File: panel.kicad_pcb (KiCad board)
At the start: 2 copper layers, 96 x 88.1 mm, 272 parts, among them J1 Terminal, J10 Terminal, J11 Conn_01x02_Socket, J12 Conn_01x02_Socket, J13 Terminal, J14 Conn_01x02_Socket, J15 Conn_01x02_Socket, J16 Terminal, J17 Conn_01x02_Socket, J18 Conn_01x02_Socket, J19 Terminal, J2 Conn_01x02_Socket, J20 Conn_01x02_Socket, J21 Conn_01x02_Socket, J22 Terminal, J23 Conn_01x02_Socket, J24 Conn_01x02_Socket, J25 Terminal, J26 Conn_01x02_Socket, J27 Conn_01x02_Socket, J28 Terminal, J29 Conn_01x02_Socket, J3 Conn_01x02_Socket, J30 Conn_01x02_Socket, J31 Terminal, J32 Conn_01x02_Socket, J33 Conn_01x02_Socket, J34 Terminal, J35 Conn_01x02_Socket, J36 Conn_01x02_Socket, J37 Terminal, J38 Conn_01x02_Socket, J39 Conn_01x02_Socket, J4 Terminal, J40 Terminal, J41 Conn_01x02_Socket, J42 Conn_01x02_Socket, J43 Terminal, J44 Conn_01x02_Socket, J45 Conn_01x02_Socket, J46 Terminal, J47 Conn_01x02_Socket, J48 Conn_01x02_Socket, J5 Conn_01x02_Socket, J6 Conn_01x02_Socket, J7 Terminal, J8 Conn_01x02_Socket, J9 Conn_01x02_Socket, M10 MountingHole_3.2mm_M3_Pad_Via, M11 MountingHole_3.2mm_M3_Pad_Via, M12 MountingHole_3.2mm_M3_Pad_Via, M13 MountingHole_3.2mm_M3_Pad_Via, M14 MountingHole_3.2mm_M3_Pad_Via, M15 MountingHole_3.2mm_M3_Pad_Via, M16 MountingHole_3.2mm_M3_Pad_Via, M17 MountingHole_3.2mm_M3_Pad_Via, M18 MountingHole_3.2mm_M3_Pad_Via, M19 MountingHole_3.2mm_M3_Pad_Via, M20 MountingHole_3.2mm_M3_Pad_Via, M21 MountingHole_3.2mm_M3_Pad_Via, M22 MountingHole_3.2mm_M3_Pad_Via, M23 MountingHole_3.2mm_M3_Pad_Via, M24 MountingHole_3.2mm_M3_Pad_Via, M25 MountingHole_3.2mm_M3_Pad_Via, M26 MountingHole_3.2mm_M3_Pad_Via, M27 MountingHole_3.2mm_M3_Pad_Via, M28 MountingHole_3.2mm_M3_Pad_Via, M29 MountingHole_3.2mm_M3_Pad_Via, M3 MountingHole_3.2mm_M3_Pad_Via, M30 MountingHole_3.2mm_M3_Pad_Via, M31 MountingHole_3.2mm_M3_Pad_Via, M32 MountingHole_3.2mm_M3_Pad_Via, M33 MountingHole_3.2mm_M3_Pad_Via, M4 MountingHole_3.2mm_M3_Pad_Via, M5 MountingHole_3.2mm_M3_Pad_Via, M6 MountingHole_3.2mm_M3_Pad_Via, M7 MountingHole_3.2mm_M3_Pad_Via, M8 MountingHole_3.2mm_M3_Pad_Via, M9 MountingHole_3.2mm_M3_Pad_Via, Q1 CSD17578Q5A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

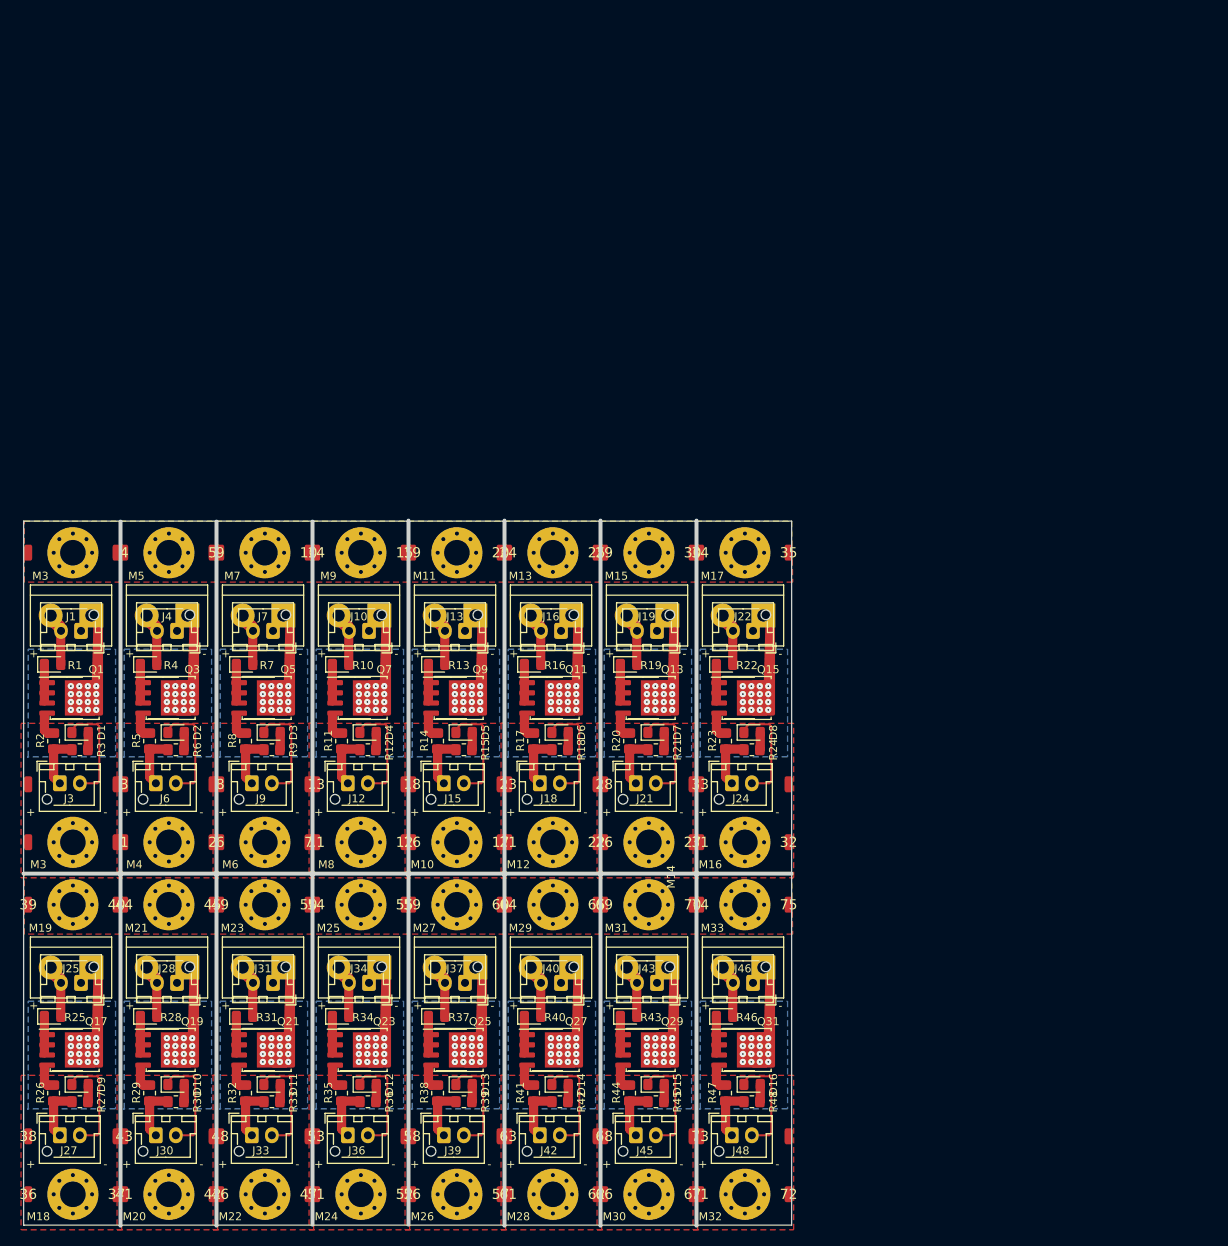
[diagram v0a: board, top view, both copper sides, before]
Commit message: update panelized PCB
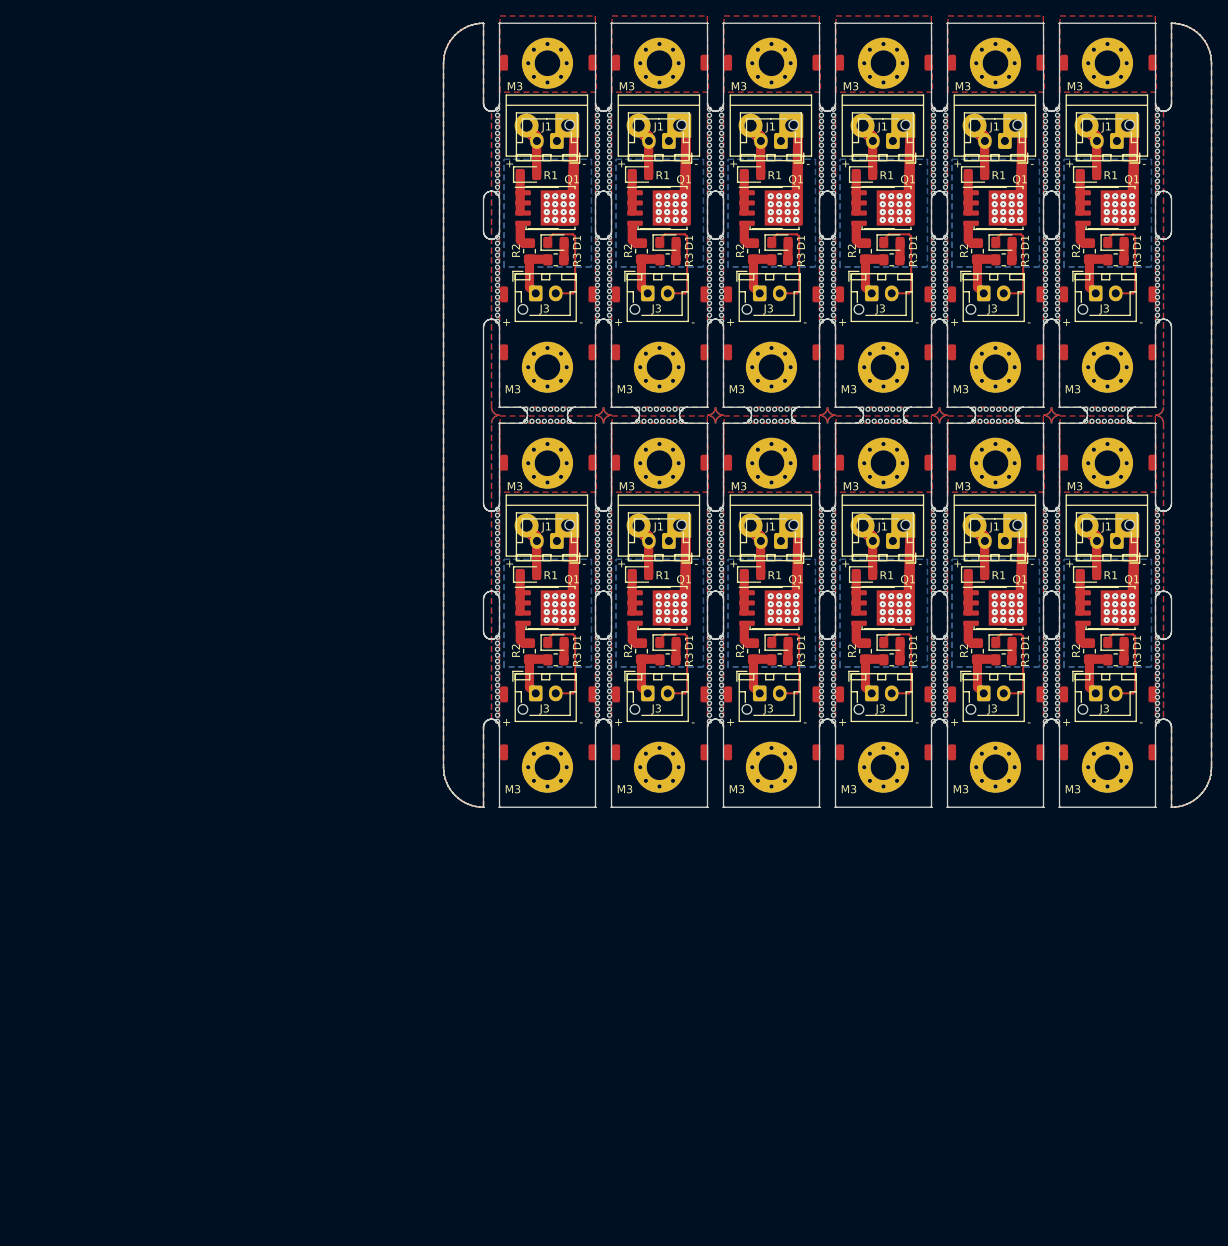
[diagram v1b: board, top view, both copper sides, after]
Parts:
- removed 1, 10, 11, 12, 13, 14, 15, 16, 17, 18, 19, 2, 20, 21, 22, 23, 24, 25, 26, 27, 28, 29, 3, 30, 31, 32, 33, 34, 35, 36, 37, 38, 39, 4, 40, 41, 42, 43, 44, 45, 46, 47, 48, 49, 5, 50, 51, 52, 53, 54, 55, 56, 57, 58, 59, 6, 60, 61, 62, 63, 64, 65, 66, 67, 68, 69, 7, 70, 71, 72, 73, 74, 75, 8, 9: , 
- removed the ? at (48.6, 122.4)
- removed the ? at (48.6, 115.1)
- removed the ? at (59.6, 122.4)
- removed the ? at (48.6, 86.2)
- removed the ? at (59.6, 86.2)
- removed the D1 at (55.1, 108.7)
- removed D10, D11, D12, D13, D14, D15, D16, D2, D3, D4, D5, D6, D7, D8, D9: LED, LED_SMD:LED_0805_2012Metric_Pad1.15x1.40mm_HandSolder
- removed the J1 at (56.5, 94.0)
- removed J10, J13, J16, J19, J22, J25, J28, J31, J34, J37, J4, J40, J43, J46, J7: Terminal, TerminalBlock:TerminalBlock_bornier-2_P5.08mm
- removed J11, J12, J14, J15, J17, J18, J20, J21, J23, J24, J26, J27, J29, J30, J32, J33, J35, J36, J38, J39, J41, J42, J44, J45, J47, J48, J5, J6, J8, J9: Conn_01x02_Socket, Connector_JST:JST_XH_B2B-XH-AM_1x02_P2.50mm_Vertical
- removed the J2 at (55.2, 96.0)
- removed the J3 at (52.5, 115.0)
- removed M10, M11, M12, M13, M14, M15, M16, M17, M18, M19, M20, M21, M22, M23, M24, M25, M26, M27, M28, M29, M30, M31, M32, M33, M4, M5, M6, M7, M8, M9: MountingHole_3.2mm_M3_Pad_Via, MountingHole:MountingHole_3.2mm_M3_Pad_Via
- removed the M3 at (54.2, 122.4)
- removed the M3 at (54.2, 86.2)
- removed the Q1 at (54.4, 104.3)
- removed Q10, Q12, Q14, Q16, Q18, Q20, Q22, Q24, Q26, Q28, Q30, Q32, Q4, Q6, Q8: CSD17578Q5A, Package_SO:SOP-8_3.76x4.96mm_P1.27mm
- removed Q11, Q13, Q15, Q17, Q19, Q21, Q23, Q25, Q27, Q29, Q3, Q31, Q5, Q7, Q9: CSD17578Q5A, Package_TO_SOT_SMD:TDSON-8-1
- removed the Q2 at (53.5, 104.3)
- removed the R1 at (51.6, 100.1)
- removed R10, R13, R16, R19, R22, R25, R28, R31, R34, R37, R4, R40, R43, R46, R7: R, LED_SMD:LED_0805_2012Metric_Pad1.15x1.40mm_HandSolder
- removed R11, R12, R14, R15, R17, R18, R20, R21, R23, R24, R26, R27, R29, R30, R32, R33, R35, R36, R38, R39, R41, R42, R44, R45, R47, R48, R5, R6, R8, R9: R, Resistor_SMD:R_0805_2012Metric_Pad1.20x1.40mm_HandSolder
- removed the R2 at (51.8, 109.7)
- removed the R3 at (55.0, 110.8)
- removed the REF** at (59.6, 115.1)
- removed REF**1, REF**10, REF**11, REF**12, REF**13, REF**14, REF**15, REF**2, REF**3, REF**4, REF**5, REF**6, REF**7, REF**8, REF**9: SolderWirePad_1x01_SMD_1x2mm, Connector_Wire:SolderWirePad_1x01_SMD_1x2mm
- added ?: , , F.Cu at (108.1, 53.9)
- added ?: , , F.Cu at (164.1, 74.9)
- added ?: , , F.Cu at (136.1, 103.9)
- added ?: , , F.Cu at (133.1, 74.9)
- added ?: , , F.Cu at (161.1, 111.1)
- added ?: , , F.Cu at (164.1, 24.9)
- added ?: , , F.Cu at (108.1, 74.9)
- added ?: , , F.Cu at (147.1, 61.1)
- added ?: , , F.Cu at (122.1, 24.9)
- added ?: , , F.Cu at (161.1, 61.1)
- added ?: , , F.Cu at (189.1, 111.1)
- added ?: , , F.Cu at (178.1, 111.1)
- added ?: , , F.Cu at (178.1, 74.9)
- added ?: , , F.Cu at (119.1, 61.1)
- added ?: , , F.Cu at (150.1, 74.9)
- added ?: , , F.Cu at (164.1, 53.9)
- added ?: , , F.Cu at (178.1, 103.9)
- added ?: , , F.Cu at (136.1, 74.9)
- added ?: , , F.Cu at (164.1, 103.9)
- added ?: , , F.Cu at (175.1, 61.1)
- added ?: , , F.Cu at (122.1, 61.1)
- added ?: , , F.Cu at (119.1, 24.9)
- added ?: , , F.Cu at (122.1, 111.1)
- added ?: , , F.Cu at (175.1, 74.9)
- added ?: , , F.Cu at (189.1, 61.1)
- added ?: , , F.Cu at (189.1, 24.9)
- added ?: , , F.Cu at (178.1, 61.1)
- added ?: , , F.Cu at (122.1, 103.9)
- added ?: , , F.Cu at (164.1, 61.1)
- added ?: , , F.Cu at (119.1, 111.1)
- added ?: , , F.Cu at (108.1, 111.1)
- added ?: , , F.Cu at (189.1, 74.9)
- added ?: , , F.Cu at (133.1, 24.9)
- added ?: , , F.Cu at (147.1, 24.9)
- added ?: , , F.Cu at (136.1, 61.1)
- added ?: , , F.Cu at (133.1, 111.1)
- added ?: , , F.Cu at (147.1, 111.1)
- added ?: , , F.Cu at (150.1, 61.1)
- added ?: , , F.Cu at (122.1, 74.9)
- added ?: , , F.Cu at (175.1, 24.9)
- added ?: , , F.Cu at (119.1, 74.9)
- added ?: , , F.Cu at (108.1, 103.9)
- added ?: , , F.Cu at (150.1, 111.1)
- added ?: , , F.Cu at (178.1, 53.9)
- added ?: , , F.Cu at (164.1, 111.1)
- added ?: , , F.Cu at (136.1, 53.9)
- added ?: , , F.Cu at (136.1, 111.1)
- added ?: , , F.Cu at (108.1, 24.9)
- added ?: , , F.Cu at (122.1, 53.9)
- added ?: , , F.Cu at (147.1, 74.9)
- added ?: , , F.Cu at (161.1, 74.9)
- added ?: , , F.Cu at (133.1, 61.1)
- added ?: , , F.Cu at (161.1, 24.9)
- added ?: , , F.Cu at (150.1, 103.9)
- added ?: , , F.Cu at (136.1, 24.9)
- added ?: , , F.Cu at (178.1, 24.9)
- added ?: , , F.Cu at (108.1, 61.1)
- added ?: , , F.Cu at (175.1, 111.1)
- added ?: , , F.Cu at (150.1, 24.9)
- added ?: , , F.Cu at (150.1, 53.9)
- added D1: LED, LED_SMD:LED_0805_2012Metric_Pad1.15x1.40mm_HandSolder, F.Cu at (114.6, 47.4)
- added D1: LED, LED_SMD:LED_0805_2012Metric_Pad1.15x1.40mm_HandSolder, F.Cu at (156.6, 97.4)
- added D1: LED, LED_SMD:LED_0805_2012Metric_Pad1.15x1.40mm_HandSolder, F.Cu at (184.6, 97.4)
- added D1: LED, LED_SMD:LED_0805_2012Metric_Pad1.15x1.40mm_HandSolder, F.Cu at (114.6, 97.4)
- added D1: LED, LED_SMD:LED_0805_2012Metric_Pad1.15x1.40mm_HandSolder, F.Cu at (170.6, 47.4)
- added D1: LED, LED_SMD:LED_0805_2012Metric_Pad1.15x1.40mm_HandSolder, F.Cu at (156.6, 47.4)
- added D1: LED, LED_SMD:LED_0805_2012Metric_Pad1.15x1.40mm_HandSolder, F.Cu at (184.6, 47.4)
- added D1: LED, LED_SMD:LED_0805_2012Metric_Pad1.15x1.40mm_HandSolder, F.Cu at (128.6, 97.4)
- added D1: LED, LED_SMD:LED_0805_2012Metric_Pad1.15x1.40mm_HandSolder, F.Cu at (142.6, 47.4)
- added D1: LED, LED_SMD:LED_0805_2012Metric_Pad1.15x1.40mm_HandSolder, F.Cu at (142.6, 97.4)
- added D1: LED, LED_SMD:LED_0805_2012Metric_Pad1.15x1.40mm_HandSolder, F.Cu at (128.6, 47.4)
- added D1: LED, LED_SMD:LED_0805_2012Metric_Pad1.15x1.40mm_HandSolder, F.Cu at (170.6, 97.4)
- added J1: Terminal, TerminalBlock:TerminalBlock_bornier-2_P5.08mm, F.Cu at (144.0, 32.8)
- added J1: Terminal, TerminalBlock:TerminalBlock_bornier-2_P5.08mm, F.Cu at (158.0, 32.8)
- added J1: Terminal, TerminalBlock:TerminalBlock_bornier-2_P5.08mm, F.Cu at (116.0, 32.8)
- added J1: Terminal, TerminalBlock:TerminalBlock_bornier-2_P5.08mm, F.Cu at (172.0, 82.8)
- added J1: Terminal, TerminalBlock:TerminalBlock_bornier-2_P5.08mm, F.Cu at (186.0, 82.8)
- added J1: Terminal, TerminalBlock:TerminalBlock_bornier-2_P5.08mm, F.Cu at (158.0, 82.8)
- added J1: Terminal, TerminalBlock:TerminalBlock_bornier-2_P5.08mm, F.Cu at (172.0, 32.8)
- added J1: Terminal, TerminalBlock:TerminalBlock_bornier-2_P5.08mm, F.Cu at (130.0, 32.8)
- added J1: Terminal, TerminalBlock:TerminalBlock_bornier-2_P5.08mm, F.Cu at (186.0, 32.8)
- added J1: Terminal, TerminalBlock:TerminalBlock_bornier-2_P5.08mm, F.Cu at (116.0, 82.8)
- added J1: Terminal, TerminalBlock:TerminalBlock_bornier-2_P5.08mm, F.Cu at (130.0, 82.8)
- added J1: Terminal, TerminalBlock:TerminalBlock_bornier-2_P5.08mm, F.Cu at (144.0, 82.8)
- added J2: Conn_01x02_Socket, Connector_JST:JST_XH_B2B-XH-AM_1x02_P2.50mm_Vertical, F.Cu at (184.7, 84.7)
- added J2: Conn_01x02_Socket, Connector_JST:JST_XH_B2B-XH-AM_1x02_P2.50mm_Vertical, F.Cu at (170.7, 34.7)
- added J2: Conn_01x02_Socket, Connector_JST:JST_XH_B2B-XH-AM_1x02_P2.50mm_Vertical, F.Cu at (128.7, 34.7)
- added J2: Conn_01x02_Socket, Connector_JST:JST_XH_B2B-XH-AM_1x02_P2.50mm_Vertical, F.Cu at (156.7, 34.7)
- added J2: Conn_01x02_Socket, Connector_JST:JST_XH_B2B-XH-AM_1x02_P2.50mm_Vertical, F.Cu at (156.7, 84.7)
- added J2: Conn_01x02_Socket, Connector_JST:JST_XH_B2B-XH-AM_1x02_P2.50mm_Vertical, F.Cu at (142.7, 84.7)
- added J2: Conn_01x02_Socket, Connector_JST:JST_XH_B2B-XH-AM_1x02_P2.50mm_Vertical, F.Cu at (114.7, 34.7)
- added J2: Conn_01x02_Socket, Connector_JST:JST_XH_B2B-XH-AM_1x02_P2.50mm_Vertical, F.Cu at (142.7, 34.7)
- added J2: Conn_01x02_Socket, Connector_JST:JST_XH_B2B-XH-AM_1x02_P2.50mm_Vertical, F.Cu at (128.7, 84.7)
- added J2: Conn_01x02_Socket, Connector_JST:JST_XH_B2B-XH-AM_1x02_P2.50mm_Vertical, F.Cu at (170.7, 84.7)
- added J2: Conn_01x02_Socket, Connector_JST:JST_XH_B2B-XH-AM_1x02_P2.50mm_Vertical, F.Cu at (114.7, 84.7)
- added J2: Conn_01x02_Socket, Connector_JST:JST_XH_B2B-XH-AM_1x02_P2.50mm_Vertical, F.Cu at (184.7, 34.7)
- added J3: Conn_01x02_Socket, Connector_JST:JST_XH_B2B-XH-AM_1x02_P2.50mm_Vertical, F.Cu at (154.0, 103.8)
- added J3: Conn_01x02_Socket, Connector_JST:JST_XH_B2B-XH-AM_1x02_P2.50mm_Vertical, F.Cu at (112.0, 103.8)
- added J3: Conn_01x02_Socket, Connector_JST:JST_XH_B2B-XH-AM_1x02_P2.50mm_Vertical, F.Cu at (112.0, 53.8)
- added J3: Conn_01x02_Socket, Connector_JST:JST_XH_B2B-XH-AM_1x02_P2.50mm_Vertical, F.Cu at (126.0, 103.8)
- added J3: Conn_01x02_Socket, Connector_JST:JST_XH_B2B-XH-AM_1x02_P2.50mm_Vertical, F.Cu at (154.0, 53.8)
- added J3: Conn_01x02_Socket, Connector_JST:JST_XH_B2B-XH-AM_1x02_P2.50mm_Vertical, F.Cu at (140.0, 53.8)
- added J3: Conn_01x02_Socket, Connector_JST:JST_XH_B2B-XH-AM_1x02_P2.50mm_Vertical, F.Cu at (168.0, 103.8)
- added J3: Conn_01x02_Socket, Connector_JST:JST_XH_B2B-XH-AM_1x02_P2.50mm_Vertical, F.Cu at (168.0, 53.8)
- added J3: Conn_01x02_Socket, Connector_JST:JST_XH_B2B-XH-AM_1x02_P2.50mm_Vertical, F.Cu at (182.0, 53.8)
- added J3: Conn_01x02_Socket, Connector_JST:JST_XH_B2B-XH-AM_1x02_P2.50mm_Vertical, F.Cu at (126.0, 53.8)
- added J3: Conn_01x02_Socket, Connector_JST:JST_XH_B2B-XH-AM_1x02_P2.50mm_Vertical, F.Cu at (140.0, 103.8)
- added J3: Conn_01x02_Socket, Connector_JST:JST_XH_B2B-XH-AM_1x02_P2.50mm_Vertical, F.Cu at (182.0, 103.8)
- added M3: MountingHole_3.2mm_M3_Pad_Via, MountingHole:MountingHole_3.2mm_M3_Pad_Via, F.Cu at (113.5, 63.0)
- added M3: MountingHole_3.2mm_M3_Pad_Via, MountingHole:MountingHole_3.2mm_M3_Pad_Via, F.Cu at (183.5, 113.0)
- added M3: MountingHole_3.2mm_M3_Pad_Via, MountingHole:MountingHole_3.2mm_M3_Pad_Via, F.Cu at (113.5, 113.0)
- added M3: MountingHole_3.2mm_M3_Pad_Via, MountingHole:MountingHole_3.2mm_M3_Pad_Via, F.Cu at (155.5, 113.0)
- added M3: MountingHole_3.2mm_M3_Pad_Via, MountingHole:MountingHole_3.2mm_M3_Pad_Via, F.Cu at (155.5, 75.0)
- added M3: MountingHole_3.2mm_M3_Pad_Via, MountingHole:MountingHole_3.2mm_M3_Pad_Via, F.Cu at (169.5, 63.0)
- added M3: MountingHole_3.2mm_M3_Pad_Via, MountingHole:MountingHole_3.2mm_M3_Pad_Via, F.Cu at (113.5, 75.0)
- added M3: MountingHole_3.2mm_M3_Pad_Via, MountingHole:MountingHole_3.2mm_M3_Pad_Via, F.Cu at (183.5, 25.0)
- added M3: MountingHole_3.2mm_M3_Pad_Via, MountingHole:MountingHole_3.2mm_M3_Pad_Via, F.Cu at (127.5, 113.0)
- added M3: MountingHole_3.2mm_M3_Pad_Via, MountingHole:MountingHole_3.2mm_M3_Pad_Via, F.Cu at (155.5, 25.0)
- added M3: MountingHole_3.2mm_M3_Pad_Via, MountingHole:MountingHole_3.2mm_M3_Pad_Via, F.Cu at (127.5, 75.0)
- added M3: MountingHole_3.2mm_M3_Pad_Via, MountingHole:MountingHole_3.2mm_M3_Pad_Via, F.Cu at (127.5, 63.0)
- added M3: MountingHole_3.2mm_M3_Pad_Via, MountingHole:MountingHole_3.2mm_M3_Pad_Via, F.Cu at (169.5, 75.0)
- added M3: MountingHole_3.2mm_M3_Pad_Via, MountingHole:MountingHole_3.2mm_M3_Pad_Via, F.Cu at (183.5, 63.0)
- added M3: MountingHole_3.2mm_M3_Pad_Via, MountingHole:MountingHole_3.2mm_M3_Pad_Via, F.Cu at (183.5, 75.0)
- added M3: MountingHole_3.2mm_M3_Pad_Via, MountingHole:MountingHole_3.2mm_M3_Pad_Via, F.Cu at (127.5, 25.0)
- added M3: MountingHole_3.2mm_M3_Pad_Via, MountingHole:MountingHole_3.2mm_M3_Pad_Via, F.Cu at (141.5, 25.0)
- added M3: MountingHole_3.2mm_M3_Pad_Via, MountingHole:MountingHole_3.2mm_M3_Pad_Via, F.Cu at (169.5, 113.0)
- added M3: MountingHole_3.2mm_M3_Pad_Via, MountingHole:MountingHole_3.2mm_M3_Pad_Via, F.Cu at (169.5, 25.0)
- added M3: MountingHole_3.2mm_M3_Pad_Via, MountingHole:MountingHole_3.2mm_M3_Pad_Via, F.Cu at (141.5, 113.0)
- added M3: MountingHole_3.2mm_M3_Pad_Via, MountingHole:MountingHole_3.2mm_M3_Pad_Via, F.Cu at (155.5, 63.0)
- added M3: MountingHole_3.2mm_M3_Pad_Via, MountingHole:MountingHole_3.2mm_M3_Pad_Via, F.Cu at (141.5, 63.0)
- added M3: MountingHole_3.2mm_M3_Pad_Via, MountingHole:MountingHole_3.2mm_M3_Pad_Via, F.Cu at (141.5, 75.0)
- added M3: MountingHole_3.2mm_M3_Pad_Via, MountingHole:MountingHole_3.2mm_M3_Pad_Via, F.Cu at (113.5, 25.0)
- added Q1: CSD17578Q5A, Package_TO_SOT_SMD:TDSON-8-1, F.Cu at (183.9, 93.1)
- added Q1: CSD17578Q5A, Package_TO_SOT_SMD:TDSON-8-1, F.Cu at (183.9, 43.1)
- added Q1: CSD17578Q5A, Package_TO_SOT_SMD:TDSON-8-1, F.Cu at (113.9, 93.1)
- added Q1: CSD17578Q5A, Package_TO_SOT_SMD:TDSON-8-1, F.Cu at (169.9, 93.1)
- added Q1: CSD17578Q5A, Package_TO_SOT_SMD:TDSON-8-1, F.Cu at (113.9, 43.1)
- added Q1: CSD17578Q5A, Package_TO_SOT_SMD:TDSON-8-1, F.Cu at (169.9, 43.1)
- added Q1: CSD17578Q5A, Package_TO_SOT_SMD:TDSON-8-1, F.Cu at (155.9, 43.1)
- added Q1: CSD17578Q5A, Package_TO_SOT_SMD:TDSON-8-1, F.Cu at (127.9, 43.1)
- added Q1: CSD17578Q5A, Package_TO_SOT_SMD:TDSON-8-1, F.Cu at (141.9, 93.1)
- added Q1: CSD17578Q5A, Package_TO_SOT_SMD:TDSON-8-1, F.Cu at (141.9, 43.1)
- added Q1: CSD17578Q5A, Package_TO_SOT_SMD:TDSON-8-1, F.Cu at (127.9, 93.1)
- added Q1: CSD17578Q5A, Package_TO_SOT_SMD:TDSON-8-1, F.Cu at (155.9, 93.1)
- added Q2: CSD17578Q5A, Package_SO:SOP-8_3.76x4.96mm_P1.27mm, F.Cu at (127.0, 93.1)
- added Q2: CSD17578Q5A, Package_SO:SOP-8_3.76x4.96mm_P1.27mm, F.Cu at (113.0, 43.1)
- added Q2: CSD17578Q5A, Package_SO:SOP-8_3.76x4.96mm_P1.27mm, F.Cu at (169.0, 43.1)
- added Q2: CSD17578Q5A, Package_SO:SOP-8_3.76x4.96mm_P1.27mm, F.Cu at (155.0, 93.1)
- added Q2: CSD17578Q5A, Package_SO:SOP-8_3.76x4.96mm_P1.27mm, F.Cu at (141.0, 43.1)
- added Q2: CSD17578Q5A, Package_SO:SOP-8_3.76x4.96mm_P1.27mm, F.Cu at (113.0, 93.1)
- added Q2: CSD17578Q5A, Package_SO:SOP-8_3.76x4.96mm_P1.27mm, F.Cu at (183.0, 43.1)
- added Q2: CSD17578Q5A, Package_SO:SOP-8_3.76x4.96mm_P1.27mm, F.Cu at (127.0, 43.1)
- added Q2: CSD17578Q5A, Package_SO:SOP-8_3.76x4.96mm_P1.27mm, F.Cu at (155.0, 43.1)
- added Q2: CSD17578Q5A, Package_SO:SOP-8_3.76x4.96mm_P1.27mm, F.Cu at (141.0, 93.1)
- added Q2: CSD17578Q5A, Package_SO:SOP-8_3.76x4.96mm_P1.27mm, F.Cu at (183.0, 93.1)
- added Q2: CSD17578Q5A, Package_SO:SOP-8_3.76x4.96mm_P1.27mm, F.Cu at (169.0, 93.1)
- added R1: R, LED_SMD:LED_0805_2012Metric_Pad1.15x1.40mm_HandSolder, F.Cu at (181.1, 88.9)
- added R1: R, LED_SMD:LED_0805_2012Metric_Pad1.15x1.40mm_HandSolder, F.Cu at (167.1, 38.9)
- added R1: R, LED_SMD:LED_0805_2012Metric_Pad1.15x1.40mm_HandSolder, F.Cu at (111.1, 88.9)
- added R1: R, LED_SMD:LED_0805_2012Metric_Pad1.15x1.40mm_HandSolder, F.Cu at (181.1, 38.9)
- added R1: R, LED_SMD:LED_0805_2012Metric_Pad1.15x1.40mm_HandSolder, F.Cu at (125.1, 88.9)
- added R1: R, LED_SMD:LED_0805_2012Metric_Pad1.15x1.40mm_HandSolder, F.Cu at (153.1, 88.9)
- added R1: R, LED_SMD:LED_0805_2012Metric_Pad1.15x1.40mm_HandSolder, F.Cu at (139.1, 88.9)
- added R1: R, LED_SMD:LED_0805_2012Metric_Pad1.15x1.40mm_HandSolder, F.Cu at (153.1, 38.9)
- added R1: R, LED_SMD:LED_0805_2012Metric_Pad1.15x1.40mm_HandSolder, F.Cu at (167.1, 88.9)
- added R1: R, LED_SMD:LED_0805_2012Metric_Pad1.15x1.40mm_HandSolder, F.Cu at (111.1, 38.9)
- added R1: R, LED_SMD:LED_0805_2012Metric_Pad1.15x1.40mm_HandSolder, F.Cu at (125.1, 38.9)
- added R1: R, LED_SMD:LED_0805_2012Metric_Pad1.15x1.40mm_HandSolder, F.Cu at (139.1, 38.9)
- added R2: R, Resistor_SMD:R_0805_2012Metric_Pad1.20x1.40mm_HandSolder, F.Cu at (153.2, 98.5)
- added R2: R, Resistor_SMD:R_0805_2012Metric_Pad1.20x1.40mm_HandSolder, F.Cu at (139.2, 98.5)
- added R2: R, Resistor_SMD:R_0805_2012Metric_Pad1.20x1.40mm_HandSolder, F.Cu at (111.2, 48.5)
- added R2: R, Resistor_SMD:R_0805_2012Metric_Pad1.20x1.40mm_HandSolder, F.Cu at (125.2, 98.5)
- added R2: R, Resistor_SMD:R_0805_2012Metric_Pad1.20x1.40mm_HandSolder, F.Cu at (167.2, 98.5)
- added R2: R, Resistor_SMD:R_0805_2012Metric_Pad1.20x1.40mm_HandSolder, F.Cu at (153.2, 48.5)
- added R2: R, Resistor_SMD:R_0805_2012Metric_Pad1.20x1.40mm_HandSolder, F.Cu at (181.2, 98.5)
- added R2: R, Resistor_SMD:R_0805_2012Metric_Pad1.20x1.40mm_HandSolder, F.Cu at (181.2, 48.5)
- added R2: R, Resistor_SMD:R_0805_2012Metric_Pad1.20x1.40mm_HandSolder, F.Cu at (139.2, 48.5)
- added R2: R, Resistor_SMD:R_0805_2012Metric_Pad1.20x1.40mm_HandSolder, F.Cu at (125.2, 48.5)
- added R2: R, Resistor_SMD:R_0805_2012Metric_Pad1.20x1.40mm_HandSolder, F.Cu at (111.2, 98.5)
- added R2: R, Resistor_SMD:R_0805_2012Metric_Pad1.20x1.40mm_HandSolder, F.Cu at (167.2, 48.5)
- added R3: R, Resistor_SMD:R_0805_2012Metric_Pad1.20x1.40mm_HandSolder, F.Cu at (156.5, 99.6)
- added R3: R, Resistor_SMD:R_0805_2012Metric_Pad1.20x1.40mm_HandSolder, F.Cu at (184.5, 99.6)
- added R3: R, Resistor_SMD:R_0805_2012Metric_Pad1.20x1.40mm_HandSolder, F.Cu at (114.5, 49.6)
- added R3: R, Resistor_SMD:R_0805_2012Metric_Pad1.20x1.40mm_HandSolder, F.Cu at (170.5, 49.6)
- added R3: R, Resistor_SMD:R_0805_2012Metric_Pad1.20x1.40mm_HandSolder, F.Cu at (128.5, 49.6)
- added R3: R, Resistor_SMD:R_0805_2012Metric_Pad1.20x1.40mm_HandSolder, F.Cu at (184.5, 49.6)
- added R3: R, Resistor_SMD:R_0805_2012Metric_Pad1.20x1.40mm_HandSolder, F.Cu at (156.5, 49.6)
- added R3: R, Resistor_SMD:R_0805_2012Metric_Pad1.20x1.40mm_HandSolder, F.Cu at (128.5, 99.6)
- added R3: R, Resistor_SMD:R_0805_2012Metric_Pad1.20x1.40mm_HandSolder, F.Cu at (114.5, 99.6)
- added R3: R, Resistor_SMD:R_0805_2012Metric_Pad1.20x1.40mm_HandSolder, F.Cu at (170.5, 99.6)
- added R3: R, Resistor_SMD:R_0805_2012Metric_Pad1.20x1.40mm_HandSolder, F.Cu at (142.5, 99.6)
- added R3: R, Resistor_SMD:R_0805_2012Metric_Pad1.20x1.40mm_HandSolder, F.Cu at (142.5, 49.6)
- added REF**: NPTH, NPTH, F.Cu at (135.2, 99.0)
- added REF**: NPTH, NPTH, F.Cu at (149.2, 107.2)
- added REF**: NPTH, NPTH, F.Cu at (143.4, 68.2)
- added REF**: NPTH, NPTH, F.Cu at (142.7, 69.8)
- added REF**: NPTH, NPTH, F.Cu at (161.8, 52.0)
- added REF**: NPTH, NPTH, F.Cu at (161.8, 39.0)
- added REF**: NPTH, NPTH, F.Cu at (107.2, 100.5)
- added REF**: NPTH, NPTH, F.Cu at (170.7, 69.8)
- added REF**: NPTH, NPTH, F.Cu at (119.8, 37.5)
- added REF**: NPTH, NPTH, F.Cu at (119.8, 88.2)
- added REF**: NPTH, NPTH, F.Cu at (161.8, 32.2)
- added REF**: NPTH, NPTH, F.Cu at (107.2, 106.5)
- added REF**: NPTH, NPTH, F.Cu at (121.2, 102.0)
- added REF**: NPTH, NPTH, F.Cu at (127.1, 69.8)
- added REF**: NPTH, NPTH, F.Cu at (177.2, 55.8)
- added REF**: SolderWirePad_1x01_SMD_1x2mm, Connector_Wire:SolderWirePad_1x01_SMD_1x2mm, F.Cu at (161.1, 53.9)
- added REF**: NPTH, NPTH, F.Cu at (163.2, 89.8)
- added REF**: NPTH, NPTH, F.Cu at (161.8, 49.0)
- added REF**: NPTH, NPTH, F.Cu at (175.8, 39.8)
- added REF**: NPTH, NPTH, F.Cu at (121.2, 52.8)
- added REF**: NPTH, NPTH, F.Cu at (163.2, 87.5)
- added REF**: NPTH, NPTH, F.Cu at (107.2, 34.5)
- added REF**: NPTH, NPTH, F.Cu at (149.2, 87.5)
- added REF**: NPTH, NPTH, F.Cu at (189.8, 87.5)
- added REF**: NPTH, NPTH, F.Cu at (119.8, 91.2)
- added REF**: NPTH, NPTH, F.Cu at (147.8, 51.2)
- added REF**: NPTH, NPTH, F.Cu at (107.2, 89.0)
- added REF**: NPTH, NPTH, F.Cu at (177.2, 49.0)
- added REF**: NPTH, NPTH, F.Cu at (158.2, 68.2)
- added REF**: NPTH, NPTH, F.Cu at (107.2, 56.5)
- added REF**: NPTH, NPTH, F.Cu at (177.2, 81.5)
- added REF**: NPTH, NPTH, F.Cu at (139.6, 69.8)
- added REF**: NPTH, NPTH, F.Cu at (121.2, 51.2)
- added REF**: NPTH, NPTH, F.Cu at (147.8, 49.0)
- added REF**: NPTH, NPTH, F.Cu at (113.1, 69.8)
- added REF**: NPTH, NPTH, F.Cu at (135.2, 51.2)
- added REF**: NPTH, NPTH, F.Cu at (189.8, 102.0)
- added REF**: NPTH, NPTH, F.Cu at (161.8, 83.8)
- added REF**: NPTH, NPTH, F.Cu at (119.8, 50.5)
- added REF**: NPTH, NPTH, F.Cu at (163.2, 88.2)
- added REF**: NPTH, NPTH, F.Cu at (107.2, 84.5)
- added REF**: NPTH, NPTH, F.Cu at (161.8, 104.2)
- added REF**: NPTH, NPTH, F.Cu at (177.2, 89.0)
- added REF**: NPTH, NPTH, F.Cu at (175.8, 36.8)
- added REF**: NPTH, NPTH, F.Cu at (133.8, 55.8)
- added REF**: NPTH, NPTH, F.Cu at (175.8, 84.5)
- added REF**: NPTH, NPTH, F.Cu at (147.8, 57.2)
- added REF**: NPTH, NPTH, F.Cu at (140.3, 68.2)
- added REF**: NPTH, NPTH, F.Cu at (119.8, 98.2)
- added REF**: NPTH, NPTH, F.Cu at (121.2, 82.2)
- added REF**: NPTH, NPTH, F.Cu at (177.2, 86.0)
- added REF**: NPTH, NPTH, F.Cu at (163.2, 52.0)
- added REF**: SolderWirePad_1x01_SMD_1x2mm, Connector_Wire:SolderWirePad_1x01_SMD_1x2mm, F.Cu at (189.1, 103.9)
- added REF**: NPTH, NPTH, F.Cu at (133.8, 81.5)
- added REF**: NPTH, NPTH, F.Cu at (135.2, 101.2)
- added REF**: NPTH, NPTH, F.Cu at (163.2, 103.5)
- added REF**: NPTH, NPTH, F.Cu at (147.8, 55.8)
- added REF**: NPTH, NPTH, F.Cu at (163.2, 48.2)
- added REF**: NPTH, NPTH, F.Cu at (147.8, 49.8)
- added REF**: NPTH, NPTH, F.Cu at (189.8, 55.8)
- added REF**: NPTH, NPTH, F.Cu at (107.2, 55.8)
- added REF**: NPTH, NPTH, F.Cu at (135.2, 36.8)
- added REF**: NPTH, NPTH, F.Cu at (133.8, 36.8)
- added REF**: NPTH, NPTH, F.Cu at (119.8, 104.2)
- added REF**: NPTH, NPTH, F.Cu at (161.8, 36.8)
- added REF**: NPTH, NPTH, F.Cu at (121.2, 88.2)
- added REF**: NPTH, NPTH, F.Cu at (147.8, 87.5)
- added REF**: NPTH, NPTH, F.Cu at (152.8, 68.2)
- added REF**: NPTH, NPTH, F.Cu at (163.2, 107.2)
- added REF**: NPTH, NPTH, F.Cu at (133.8, 54.2)
- added REF**: NPTH, NPTH, F.Cu at (119.8, 55.8)
- added REF**: NPTH, NPTH, F.Cu at (121.2, 83.0)
- added REF**: NPTH, NPTH, F.Cu at (107.2, 39.8)
- added REF**: NPTH, NPTH, F.Cu at (119.8, 30.8)
- added REF**: NPTH, NPTH, F.Cu at (107.2, 38.2)
- added REF**: NPTH, NPTH, F.Cu at (161.8, 86.8)
- added REF**: NPTH, NPTH, F.Cu at (141.9, 68.2)
- added REF**: NPTH, NPTH, F.Cu at (147.8, 96.8)
- added REF**: NPTH, NPTH, F.Cu at (163.2, 37.5)
- added REF**: NPTH, NPTH, F.Cu at (107.2, 86.8)
- added REF**: NPTH, NPTH, F.Cu at (119.8, 102.0)
- added REF**: NPTH, NPTH, F.Cu at (163.2, 47.5)
- added REF**: NPTH, NPTH, F.Cu at (163.2, 82.2)
- added REF**: NPTH, NPTH, F.Cu at (189.8, 39.0)
- added REF**: NPTH, NPTH, F.Cu at (113.9, 69.8)
- added REF**: SolderWirePad_1x01_SMD_1x2mm, Connector_Wire:SolderWirePad_1x01_SMD_1x2mm, F.Cu at (161.1, 103.9)
- added REF**: NPTH, NPTH, F.Cu at (121.2, 55.8)
- added REF**: NPTH, NPTH, F.Cu at (183.1, 68.2)
- added REF**: NPTH, NPTH, F.Cu at (161.8, 102.0)
- added REF**: NPTH, NPTH, F.Cu at (121.2, 80.8)
- added REF**: NPTH, NPTH, F.Cu at (133.8, 89.0)
- added REF**: NPTH, NPTH, F.Cu at (119.8, 96.8)
- added REF**: NPTH, NPTH, F.Cu at (177.2, 86.8)
- added REF**: NPTH, NPTH, F.Cu at (189.8, 49.8)
- added REF**: NPTH, NPTH, F.Cu at (107.2, 32.2)
- added REF**: NPTH, NPTH, F.Cu at (149.2, 99.8)
- added REF**: NPTH, NPTH, F.Cu at (119.8, 86.8)
- added REF**: NPTH, NPTH, F.Cu at (175.8, 105.8)
- added REF**: NPTH, NPTH, F.Cu at (175.8, 86.0)
- added REF**: NPTH, NPTH, F.Cu at (135.2, 53.5)
- added REF**: NPTH, NPTH, F.Cu at (147.8, 55.0)
- added REF**: NPTH, NPTH, F.Cu at (189.8, 99.0)
- added REF**: SolderWirePad_1x01_SMD_1x2mm, Connector_Wire:SolderWirePad_1x01_SMD_1x2mm, F.Cu at (119.1, 53.9)
- added REF**: NPTH, NPTH, F.Cu at (149.2, 56.5)
- added REF**: NPTH, NPTH, F.Cu at (121.2, 86.0)
- added REF**: NPTH, NPTH, F.Cu at (149.2, 102.8)
- added REF**: NPTH, NPTH, F.Cu at (149.2, 49.0)
- added REF**: NPTH, NPTH, F.Cu at (147.8, 52.8)
- added REF**: NPTH, NPTH, F.Cu at (133.8, 105.8)
- added REF**: NPTH, NPTH, F.Cu at (107.2, 99.0)
- added REF**: NPTH, NPTH, F.Cu at (147.8, 84.5)
- added REF**: NPTH, NPTH, F.Cu at (121.2, 34.5)
- added REF**: NPTH, NPTH, F.Cu at (175.8, 41.2)
- added REF**: NPTH, NPTH, F.Cu at (149.2, 52.8)
- added REF**: NPTH, NPTH, F.Cu at (135.2, 55.8)
- added REF**: NPTH, NPTH, F.Cu at (133.8, 83.0)
- added REF**: NPTH, NPTH, F.Cu at (119.8, 39.0)
- added REF**: NPTH, NPTH, F.Cu at (161.8, 84.5)
- added REF**: NPTH, NPTH, F.Cu at (177.2, 82.2)
- added REF**: NPTH, NPTH, F.Cu at (155.1, 69.8)
- added REF**: NPTH, NPTH, F.Cu at (147.8, 33.0)
- added REF**: NPTH, NPTH, F.Cu at (135.2, 103.5)
- added REF**: NPTH, NPTH, F.Cu at (163.2, 105.8)
- added REF**: NPTH, NPTH, F.Cu at (135.2, 107.2)
- added REF**: NPTH, NPTH, F.Cu at (147.8, 102.8)
- added REF**: NPTH, NPTH, F.Cu at (163.2, 84.5)
- added REF**: NPTH, NPTH, F.Cu at (121.2, 39.8)
- added REF**: NPTH, NPTH, F.Cu at (185.4, 68.2)
- added REF**: NPTH, NPTH, F.Cu at (163.2, 52.8)
- added REF**: NPTH, NPTH, F.Cu at (175.8, 98.2)
- added REF**: NPTH, NPTH, F.Cu at (128.7, 69.8)
- added REF**: NPTH, NPTH, F.Cu at (177.2, 41.2)
- added REF**: NPTH, NPTH, F.Cu at (175.8, 83.0)
- added REF**: NPTH, NPTH, F.Cu at (163.2, 32.2)
- added REF**: NPTH, NPTH, F.Cu at (119.8, 105.0)
- added REF**: NPTH, NPTH, F.Cu at (119.8, 99.0)
- added REF**: NPTH, NPTH, F.Cu at (152.8, 69.8)
- added REF**: NPTH, NPTH, F.Cu at (133.8, 88.2)
- added REF**: NPTH, NPTH, F.Cu at (133.8, 40.5)
- added REF**: NPTH, NPTH, F.Cu at (135.2, 85.2)
- added REF**: NPTH, NPTH, F.Cu at (121.2, 86.8)
- added REF**: NPTH, NPTH, F.Cu at (175.8, 38.2)
- added REF**: NPTH, NPTH, F.Cu at (163.2, 55.0)
- added REF**: NPTH, NPTH, F.Cu at (133.8, 46.8)
- added REF**: NPTH, NPTH, F.Cu at (154.3, 69.8)
- added REF**: NPTH, NPTH, F.Cu at (141.1, 68.2)
- added REF**: NPTH, NPTH, F.Cu at (133.8, 36.0)
- added REF**: NPTH, NPTH, F.Cu at (189.8, 99.8)
- added REF**: NPTH, NPTH, F.Cu at (147.8, 30.8)
- added REF**: NPTH, NPTH, F.Cu at (121.2, 85.2)
- added REF**: NPTH, NPTH, F.Cu at (168.3, 68.2)
- added REF**: NPTH, NPTH, F.Cu at (119.8, 33.0)
- added REF**: NPTH, NPTH, F.Cu at (189.8, 40.5)
- added REF**: NPTH, NPTH, F.Cu at (135.2, 34.5)
- added REF**: NPTH, NPTH, F.Cu at (107.2, 90.5)
- added REF**: NPTH, NPTH, F.Cu at (135.2, 105.0)
- added REF**: NPTH, NPTH, F.Cu at (133.8, 49.0)
- added REF**: NPTH, NPTH, F.Cu at (189.8, 35.2)
- added REF**: NPTH, NPTH, F.Cu at (189.8, 32.2)
- added REF**: NPTH, NPTH, F.Cu at (133.8, 39.0)
- added REF**: NPTH, NPTH, F.Cu at (125.6, 69.8)
- added REF**: NPTH, NPTH, F.Cu at (183.9, 69.8)
- added REF**: NPTH, NPTH, F.Cu at (189.8, 96.8)
- added REF**: NPTH, NPTH, F.Cu at (135.2, 84.5)
- added REF**: NPTH, NPTH, F.Cu at (163.2, 81.5)
- added REF**: NPTH, NPTH, F.Cu at (149.2, 49.8)
- added REF**: NPTH, NPTH, F.Cu at (133.8, 97.5)
- added REF**: NPTH, NPTH, F.Cu at (133.8, 47.5)
- added REF**: NPTH, NPTH, F.Cu at (133.8, 41.2)
- added REF**: NPTH, NPTH, F.Cu at (121.2, 99.0)
- added REF**: NPTH, NPTH, F.Cu at (189.8, 85.2)
- added REF**: NPTH, NPTH, F.Cu at (175.8, 102.8)
- added REF**: NPTH, NPTH, F.Cu at (175.8, 80.8)
- added REF**: NPTH, NPTH, F.Cu at (135.2, 33.8)
- added REF**: NPTH, NPTH, F.Cu at (163.2, 39.8)
- added REF**: NPTH, NPTH, F.Cu at (135.2, 49.8)
- added REF**: NPTH, NPTH, F.Cu at (177.2, 102.8)
- added REF**: NPTH, NPTH, F.Cu at (124.8, 69.8)
- added REF**: SolderWirePad_1x01_SMD_1x2mm, Connector_Wire:SolderWirePad_1x01_SMD_1x2mm, F.Cu at (119.1, 103.9)
- added REF**: NPTH, NPTH, F.Cu at (121.2, 101.2)
- added REF**: NPTH, NPTH, F.Cu at (177.2, 100.5)
- added REF**: NPTH, NPTH, F.Cu at (121.2, 33.8)
- added REF**: NPTH, NPTH, F.Cu at (135.2, 102.0)
- added REF**: NPTH, NPTH, F.Cu at (135.2, 100.5)
- added REF**: NPTH, NPTH, F.Cu at (133.8, 84.5)
- added REF**: NPTH, NPTH, F.Cu at (189.8, 102.8)
- added REF**: NPTH, NPTH, F.Cu at (139.6, 68.2)
- added REF**: NPTH, NPTH, F.Cu at (135.2, 82.2)
- added REF**: NPTH, NPTH, F.Cu at (149.2, 39.8)
- added REF**: NPTH, NPTH, F.Cu at (133.8, 99.8)
- added REF**: NPTH, NPTH, F.Cu at (161.8, 36.0)
- added REF**: NPTH, NPTH, F.Cu at (189.8, 84.5)
- added REF**: NPTH, NPTH, F.Cu at (161.8, 82.2)
- added REF**: NPTH, NPTH, F.Cu at (107.2, 91.2)
- added REF**: NPTH, NPTH, F.Cu at (161.8, 54.2)
- added REF**: NPTH, NPTH, F.Cu at (121.2, 37.5)
- added REF**: NPTH, NPTH, F.Cu at (177.2, 55.0)
- added REF**: NPTH, NPTH, F.Cu at (133.8, 51.2)
- added REF**: NPTH, NPTH, F.Cu at (163.2, 36.8)
- added REF**: NPTH, NPTH, F.Cu at (149.2, 100.5)
- added REF**: NPTH, NPTH, F.Cu at (135.2, 55.0)
- added REF**: NPTH, NPTH, F.Cu at (180.8, 69.8)
- added REF**: NPTH, NPTH, F.Cu at (177.2, 84.5)
- added REF**: NPTH, NPTH, F.Cu at (149.2, 50.5)
- added REF**: NPTH, NPTH, F.Cu at (161.8, 107.2)
- added REF**: NPTH, NPTH, F.Cu at (121.2, 47.5)
- added REF**: NPTH, NPTH, F.Cu at (135.2, 97.5)
- added REF**: NPTH, NPTH, F.Cu at (119.8, 103.5)
- added REF**: NPTH, NPTH, F.Cu at (163.2, 56.5)
- added REF**: NPTH, NPTH, F.Cu at (119.8, 55.0)
- added REF**: NPTH, NPTH, F.Cu at (161.8, 57.2)
- added REF**: NPTH, NPTH, F.Cu at (135.2, 83.8)
- added REF**: NPTH, NPTH, F.Cu at (163.2, 101.2)
- added REF**: NPTH, NPTH, F.Cu at (163.2, 80.8)
- added REF**: NPTH, NPTH, F.Cu at (135.2, 86.0)
- added REF**: NPTH, NPTH, F.Cu at (107.2, 82.2)
- added REF**: NPTH, NPTH, F.Cu at (121.2, 105.0)
- added REF**: NPTH, NPTH, F.Cu at (147.8, 102.0)
- added REF**: NPTH, NPTH, F.Cu at (107.2, 104.2)
- added REF**: NPTH, NPTH, F.Cu at (119.8, 35.2)
- added REF**: NPTH, NPTH, F.Cu at (147.8, 89.8)
- added REF**: NPTH, NPTH, F.Cu at (133.8, 102.0)
- added REF**: NPTH, NPTH, F.Cu at (149.2, 98.2)
- added REF**: NPTH, NPTH, F.Cu at (161.8, 90.5)
- added REF**: NPTH, NPTH, F.Cu at (147.8, 86.8)
- added REF**: NPTH, NPTH, F.Cu at (147.8, 97.5)
- added REF**: NPTH, NPTH, F.Cu at (189.8, 105.8)
- added REF**: NPTH, NPTH, F.Cu at (126.3, 68.2)
- added REF**: NPTH, NPTH, F.Cu at (119.8, 102.8)
- added REF**: NPTH, NPTH, F.Cu at (149.2, 89.0)
- added REF**: NPTH, NPTH, F.Cu at (177.2, 39.0)
- added REF**: NPTH, NPTH, F.Cu at (175.8, 33.8)
- added REF**: NPTH, NPTH, F.Cu at (149.2, 105.8)
- added REF**: NPTH, NPTH, F.Cu at (177.2, 32.2)
- added REF**: NPTH, NPTH, F.Cu at (163.2, 35.2)
- added REF**: NPTH, NPTH, F.Cu at (186.2, 69.8)
- added REF**: NPTH, NPTH, F.Cu at (133.8, 105.0)
- added REF**: NPTH, NPTH, F.Cu at (175.8, 52.0)
- added REF**: NPTH, NPTH, F.Cu at (114.7, 68.2)
- added REF**: NPTH, NPTH, F.Cu at (163.2, 89.0)
- added REF**: NPTH, NPTH, F.Cu at (161.8, 105.8)
- added REF**: NPTH, NPTH, F.Cu at (107.2, 53.5)
- added REF**: NPTH, NPTH, F.Cu at (161.8, 33.8)
- added REF**: NPTH, NPTH, F.Cu at (107.2, 51.2)
- added REF**: NPTH, NPTH, F.Cu at (121.2, 103.5)
- added REF**: NPTH, NPTH, F.Cu at (147.8, 82.2)
- added REF**: NPTH, NPTH, F.Cu at (163.2, 86.8)
- added REF**: NPTH, NPTH, F.Cu at (181.6, 69.8)
- added REF**: NPTH, NPTH, F.Cu at (107.2, 105.8)
- added REF**: NPTH, NPTH, F.Cu at (177.2, 98.2)
- added REF**: NPTH, NPTH, F.Cu at (133.8, 83.8)
- added REF**: NPTH, NPTH, F.Cu at (177.2, 87.5)
- added REF**: NPTH, NPTH, F.Cu at (155.9, 68.2)
- added REF**: NPTH, NPTH, F.Cu at (116.2, 69.8)
- added REF**: NPTH, NPTH, F.Cu at (144.2, 69.8)
- added REF**: NPTH, NPTH, F.Cu at (163.2, 40.5)
- added REF**: NPTH, NPTH, F.Cu at (175.8, 105.0)
- added REF**: NPTH, NPTH, F.Cu at (107.2, 99.8)
- added REF**: NPTH, NPTH, F.Cu at (177.2, 102.0)
- added REF**: NPTH, NPTH, F.Cu at (189.8, 41.2)
- added REF**: NPTH, NPTH, F.Cu at (167.6, 68.2)
- added REF**: NPTH, NPTH, F.Cu at (149.2, 82.2)
- added REF**: NPTH, NPTH, F.Cu at (135.2, 52.0)
- added REF**: NPTH, NPTH, F.Cu at (129.4, 68.2)
- added REF**: NPTH, NPTH, F.Cu at (158.2, 69.8)
- added REF**: NPTH, NPTH, F.Cu at (121.2, 104.2)
- added REF**: NPTH, NPTH, F.Cu at (177.2, 103.5)
- added REF**: NPTH, NPTH, F.Cu at (163.2, 53.5)
- added REF**: NPTH, NPTH, F.Cu at (163.2, 55.8)
- added REF**: NPTH, NPTH, F.Cu at (177.2, 52.8)
- added REF**: NPTH, NPTH, F.Cu at (149.2, 85.2)
- added REF**: NPTH, NPTH, F.Cu at (147.8, 36.0)
- added REF**: NPTH, NPTH, F.Cu at (189.8, 104.2)
- added REF**: NPTH, NPTH, F.Cu at (175.8, 55.0)
- added REF**: NPTH, NPTH, F.Cu at (161.8, 80.8)
- added REF**: NPTH, NPTH, F.Cu at (107.2, 37.5)
- added REF**: NPTH, NPTH, F.Cu at (189.8, 33.8)
- added REF**: NPTH, NPTH, F.Cu at (163.2, 33.0)
- added REF**: NPTH, NPTH, F.Cu at (161.8, 89.8)
- added REF**: NPTH, NPTH, F.Cu at (147.8, 105.8)
- added REF**: NPTH, NPTH, F.Cu at (149.2, 34.5)
- added REF**: NPTH, NPTH, F.Cu at (119.8, 105.8)
- added REF**: NPTH, NPTH, F.Cu at (161.8, 102.8)
- added REF**: SolderWirePad_1x01_SMD_1x2mm, Connector_Wire:SolderWirePad_1x01_SMD_1x2mm, F.Cu at (147.1, 53.9)
- added REF**: NPTH, NPTH, F.Cu at (135.2, 89.8)
- added REF**: NPTH, NPTH, F.Cu at (163.2, 33.8)
- added REF**: NPTH, NPTH, F.Cu at (107.2, 81.5)
- added REF**: NPTH, NPTH, F.Cu at (149.2, 96.8)
- added REF**: NPTH, NPTH, F.Cu at (161.8, 40.5)
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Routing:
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- added copper zone on B.Cu, net (none)
- added copper zone on F.Cu, net (none)
- added copper zone on F.Cu, net Board_0-GND
- added copper zone on B.Cu, net Board_0-Net-(J1-Pin_1)
- added copper zone on F.Cu, net Board_1-GND
- added copper zone on B.Cu, net Board_1-Net-(J1-Pin_1)
- added copper zone on F.Cu, net Board_10-GND
- added copper zone on B.Cu, net Board_10-Net-(J1-Pin_1)
- added copper zone on F.Cu, net Board_11-GND
- added copper zone on B.Cu, net Board_11-Net-(J1-Pin_1)
- added copper zone on F.Cu, net Board_2-GND
- added copper zone on B.Cu, net Board_2-Net-(J1-Pin_1)
- added copper zone on F.Cu, net Board_3-GND
- added copper zone on B.Cu, net Board_3-Net-(J1-Pin_1)
- added copper zone on F.Cu, net Board_4-GND
- added copper zone on B.Cu, net Board_4-Net-(J1-Pin_1)
- added copper zone on F.Cu, net Board_5-GND
- added copper zone on B.Cu, net Board_5-Net-(J1-Pin_1)
- added copper zone on F.Cu, net Board_6-GND
- added copper zone on B.Cu, net Board_6-Net-(J1-Pin_1)
- added copper zone on F.Cu, net Board_7-GND
- added copper zone on B.Cu, net Board_7-Net-(J1-Pin_1)
- added copper zone on F.Cu, net Board_8-GND
- added copper zone on B.Cu, net Board_8-Net-(J1-Pin_1)
- added copper zone on F.Cu, net Board_9-GND
- added copper zone on B.Cu, net Board_9-Net-(J1-Pin_1)
- removed copper zone on F.Cu, net GND
- removed copper zone on B.Cu, net Net-(J1-Pin_1)
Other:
- board size 96 x 88.1 mm -> 96 x 98 mm
- board text removed: "<- V-Cut"
